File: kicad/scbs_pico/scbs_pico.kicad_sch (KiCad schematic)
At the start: 64 parts, among them J1 Conn_01x06_Male, J2 Conn_ARM_JTAG_SWD_10, Q1 2N2907, Q2 2N7002, Q3 MMBT3904, Q4 MMBT3904, U1 TLV9062xD, U2 PC817, U3 Pico

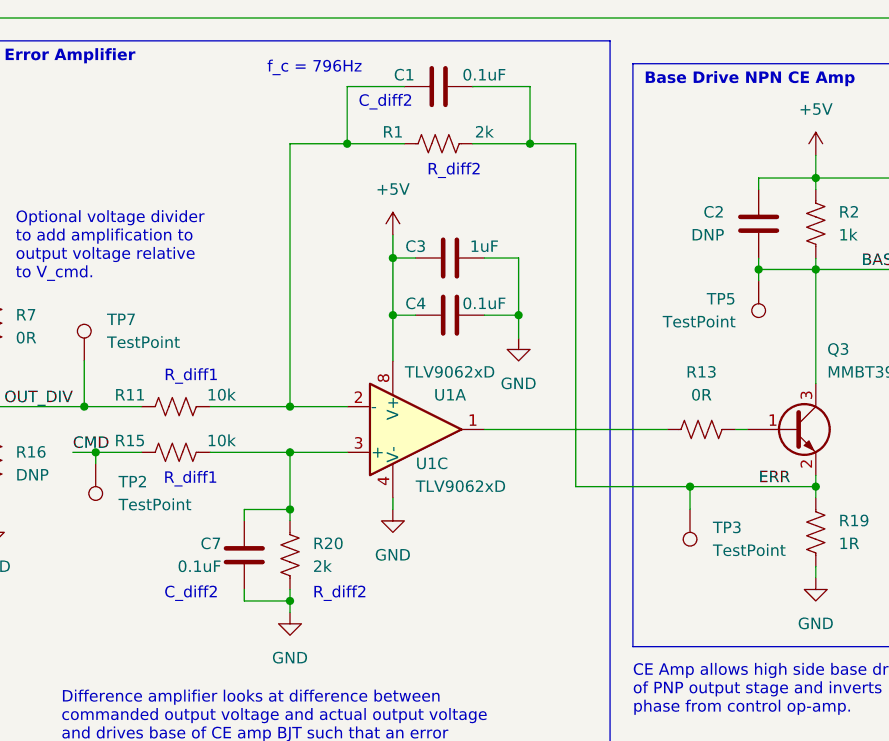
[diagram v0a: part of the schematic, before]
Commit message: Add calibrated output voltage setting
* Python script serial utility for sending DIS, MWR, MRD commands to
  device.
* Three-coefficient polynomial calibration implemented in firmware for
  closer matching of output voltage (looks pretty darn good)! Makes up
  for the crappiness / non-linearity of the PWM pseudo-DAC driving a
  load without a buffer.
* Connecting the plumbing for setting output voltage via serial in the
  SCBS firmware.
* Clean up some commented code garbage that was lying around.
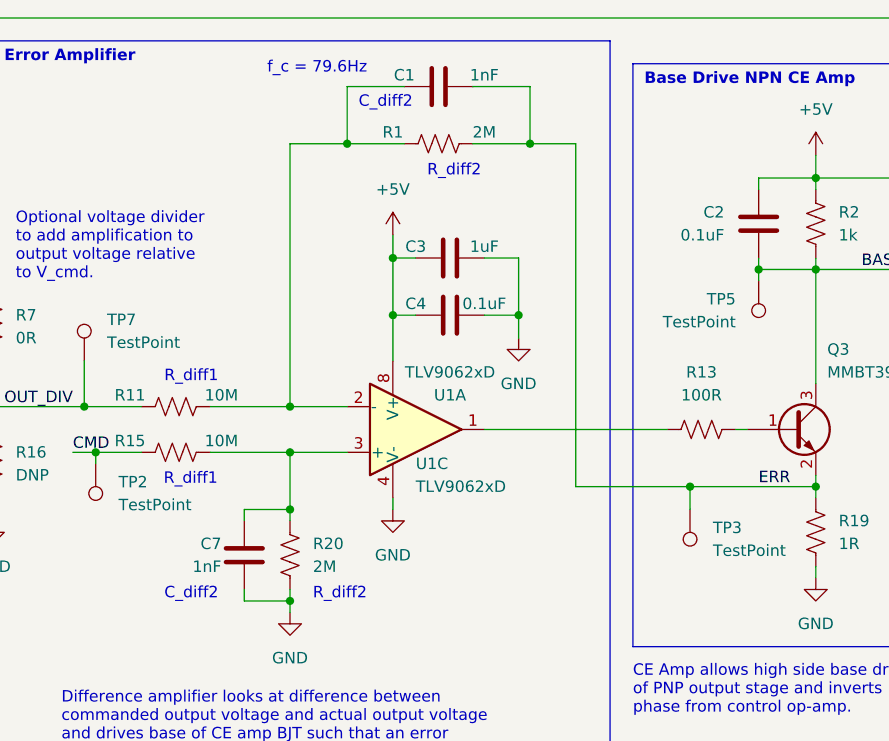
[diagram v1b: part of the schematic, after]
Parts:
- C1, C7: value 0.1uF -> 1nF
- C2: value DNP -> 0.1uF
- R1, R20: value 2k -> 2M
- R11, R15: value 10k -> 10M
- R13: value 0R -> 100R
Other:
- note added: "f_c = 79.6Hz"
- note removed: "f_c = 796Hz"
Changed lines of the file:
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@@
     (effects (font (size 1.27 1.27) bold) (justify left bottom))
   )
-  (text "f_c = 796Hz" (at 203.2 38.1 0)
+  (text "f_c = 79.6Hz" (at 203.2 38.1 0)
     (effects (font (size 1.27 1.27)) (justify left bottom))
   )
@@
     (in_bom yes) (on_board yes) (fields_autoplaced)
     (property "Reference" "R13" (id 0) (at 251.46 71.12 90))
-    (property "Value" "0R" (id 1) (at 251.46 73.66 90))
+    (property "Value" "100R" (id 1) (at 251.46 73.66 90))
     (property "Footprint" "Resistor_SMD:R_0805_2012Metric" (id 2) (at 251.714 76.454 90)
       (effects (font (size 1.27 1.27)) hide)
@@
     (in_bom yes) (on_board yes)
     (property "Reference" "C1" (id 0) (at 218.44 38.1 90))
-    (property "Value" "0.1uF" (id 1) (at 227.33 38.1 90))
+    (property "Value" "1nF" (id 1) (at 227.33 38.1 90))
     (property "Footprint" "Capacitor_SMD:C_0805_2012Metric" (id 2) (at 226.06 38.4048 0)
       (effects (font (size 1.27 1.27)) hide)
@@
     (in_bom yes) (on_board yes)
     (property "Reference" "R15" (id 0) (at 187.96 78.74 90))
-    (property "Value" "10k" (id 1) (at 198.12 78.74 90))
+    (property "Value" "10M" (id 1) (at 198.12 78.74 90))
     (property "Footprint" "Resistor_SMD:R_0805_2012Metric" (id 2) (at 193.294 78.994 90)
       (effects (font (size 1.27 1.27)) hide)
@@
     (in_bom yes) (on_board yes)
     (property "Reference" "R11" (id 0) (at 187.96 73.66 90))
-    (property "Value" "10k" (id 1) (at 198.12 73.66 90))
+    (property "Value" "10M" (id 1) (at 198.12 73.66 90))
     (property "Footprint" "Resistor_SMD:R_0805_2012Metric" (id 2) (at 193.294 73.914 90)
       (effects (font (size 1.27 1.27)) hide)
@@
       (effects (font (size 1.27 1.27)) (justify right))
     )
-    (property "Value" "0.1uF" (id 1) (at 198.12 92.71 0)
+    (property "Value" "1nF" (id 1) (at 198.12 92.71 0)
       (effects (font (size 1.27 1.27)) (justify right))
     )
@@
     (in_bom yes) (on_board yes)
     (property "Reference" "R1" (id 0) (at 217.17 44.45 90))
-    (property "Value" "2k" (id 1) (at 227.33 44.45 90))
+    (property "Value" "2M" (id 1) (at 227.33 44.45 90))
     (property "Footprint" "Resistor_SMD:R_0805_2012Metric" (id 2) (at 222.504 44.704 90)
       (effects (font (size 1.27 1.27)) hide)
@@
       (effects (font (size 1.27 1.27)) (justify left))
     )
-    (property "Value" "2k" (id 1) (at 208.28 92.7099 0)
+    (property "Value" "2M" (id 1) (at 208.28 92.7099 0)
       (effects (font (size 1.27 1.27)) (justify left))
     )
@@
       (effects (font (size 1.27 1.27)) (justify right))
     )
-    (property "Value" "DNP" (id 1) (at 254 55.88 0)
+    (property "Value" "0.1uF" (id 1) (at 254 55.88 0)
       (effects (font (size 1.27 1.27)) (justify right))
     )
@@
     )
     (path "/501c76a6-d2b9-4bd2-89b6-22fe1a20bdf8"
-      (reference "C1") (unit 1) (value "0.1uF") (footprint "Capacitor_SMD:C_0805_2012Metric")
+      (reference "C1") (unit 1) (value "1nF") (footprint "Capacitor_SMD:C_0805_2012Metric")
     )
     (path "/ea657372-77a3-4b71-8e5f-768a7eedd395"
-      (reference "C2") (unit 1) (value "DNP") (footprint "Capacitor_SMD:C_0805_2012Metric")
+      (reference "C2") (unit 1) (value "0.1uF") (footprint "Capacitor_SMD:C_0805_2012Metric")
     )
     (path "/81879832-ef3a-4d07-bc20-d7739a2f0b44"
@@
     )
     (path "/9977a2d0-eb1e-4053-9401-7449ac849cb7"
-      (reference "C7") (unit 1) (value "0.1uF") (footprint "Capacitor_SMD:C_0805_2012Metric")
+      (reference "C7") (unit 1) (value "1nF") (footprint "Capacitor_SMD:C_0805_2012Metric")
     )
     (path "/44978827-6e8d-4181-bf69-4f56262ac5b3"
@@
     )
     (path "/9df6450b-426e-44a8-8013-a148bb9d7476"
-      (reference "R1") (unit 1) (value "2k") (footprint "Resistor_SMD:R_0805_2012Metric")
+      (reference "R1") (unit 1) (value "2M") (footprint "Resistor_SMD:R_0805_2012Metric")
     )
     (path "/996fc4c6-670c-47e0-8fd9-40439fd4e145"
@@
     )
     (path "/89e2b305-09b7-42be-a849-0b21d2a4259b"
-      (reference "R11") (unit 1) (value "10k") (footprint "Resistor_SMD:R_0805_2012Metric")
+      (reference "R11") (unit 1) (value "10M") (footprint "Resistor_SMD:R_0805_2012Metric")
     )
     (path "/ff8d37cd-3da3-417c-a0fc-f4fdf44a9126"
@@
     )
     (path "/3da06448-3f74-4948-a6de-8e4ddcf3a451"
-      (reference "R13") (unit 1) (value "0R") (footprint "Resistor_SMD:R_0805_2012Metric")
+      (reference "R13") (unit 1) (value "100R") (footprint "Resistor_SMD:R_0805_2012Metric")
     )
     (path "/01aaca7e-4af3-469d-90de-3e450da96ed7"
@@
     )
     (path "/85853062-8be8-409c-8854-83e4a8ae9bfe"
-      (reference "R15") (unit 1) (value "10k") (footprint "Resistor_SMD:R_0805_2012Metric")
+      (reference "R15") (unit 1) (value "10M") (footprint "Resistor_SMD:R_0805_2012Metric")
     )
     (path "/59a896a2-1a0f-4726-81bd-86b5c1073d52"
@@
     )
     (path "/9f1e2e01-723a-446f-8f13-e29292866f46"
-      (reference "R20") (unit 1) (value "2k") (footprint "Resistor_SMD:R_0805_2012Metric")
+      (reference "R20") (unit 1) (value "2M") (footprint "Resistor_SMD:R_0805_2012Metric")
     )
     (path "/fc0f4a6b-8c97-40be-a956-b8dcc5258115"

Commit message: Add SCBS array PCBA Rev A
* Update design notebook.
* Export some stuff for SCBS Pico.
* Create SCBS Array motherboard.
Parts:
- added C?: 10uF 16V, symbol Device:C_Polarized_US
- C2: value 0.1uF -> DNP
- R5: value 100R -> 750R
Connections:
- net GND: now also C?.2
- net OUT: now also C?.1
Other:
- note added: "Output Cap (Electrolytic)"
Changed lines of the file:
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@@
   (junction (at 295.91 83.82) (diameter 0) (color 0 0 0 0)
   )
+  (junction (at 379.73 69.85) (diameter 0) (color 0 0 0 0)
+  )
   (junction (at 341.63 116.84) (diameter 0) (color 0 0 0 0)
   )
@@
     (stroke (width 0) (type default) (color 0 0 0 0))
   )
+  (wire (pts (xy 379.73 80.01) (xy 379.73 82.55))
+    (stroke (width 0) (type default) (color 0 0 0 0))
+  )
   (wire (pts (xy 168.91 171.45) (xy 168.91 170.18))
     (stroke (width 0) (type default) (color 0 0 0 0))
@@
     (stroke (width 0) (type default) (color 0 0 0 0))
   )
-  (wire (pts (xy 374.65 69.85) (xy 388.62 69.85))
+  (wire (pts (xy 374.65 69.85) (xy 379.73 69.85))
     (stroke (width 0) (type default) (color 0 0 0 0))
   )
@@
     (stroke (width 0) (type default) (color 0 0 0 0))
   )
+  (wire (pts (xy 379.73 69.85) (xy 388.62 69.85))
+    (stroke (width 0) (type default) (color 0 0 0 0))
+  )
   (wire (pts (xy 217.17 55.88) (xy 217.17 58.42))
     (stroke (width 0) (type default) (color 0 0 0 0))
@@
     (stroke (width 0) (type default) (color 0 0 0 0))
   )
+  (wire (pts (xy 379.73 69.85) (xy 379.73 72.39))
+    (stroke (width 0) (type default) (color 0 0 0 0))
+  )
   (wire (pts (xy 111.76 104.14) (xy 114.3 104.14))
     (stroke (width 0) (type default) (color 0 0 0 0))
@@
     (effects (font (size 1.27 1.27)) (justify left bottom))
   )
+  (text "Output Cap\n(Electrolytic)" (at 383.54 82.55 0)
+    (effects (font (size 1.27 1.27)) (justify left bottom))
+  )
   (text "I_f = 10mA for >100% CTR\nV_f = 1.2V" (at 104.14 95.25 0)
     (effects (font (size 1.27 1.27)) (justify left bottom))
@@
     (in_bom yes) (on_board yes) (fields_autoplaced)
     (property "Reference" "R5" (id 0) (at 283.21 53.34 90))
-    (property "Value" "100R" (id 1) (at 283.21 55.88 90))
+    (property "Value" "750R" (id 1) (at 283.21 55.88 90))
     (property "Footprint" "Resistor_SMD:R_0805_2012Metric" (id 2) (at 283.464 58.674 90)
       (effects (font (size 1.27 1.27)) hide)
@@
     (pin "1")
   )
+  (symbol (lib_id "Device:C_Polarized_US") (at 379.73 76.2 0) (unit 1)
+    (in_bom yes) (on_board yes) (fields_autoplaced)
+    (property "Reference" "C?" (id 0) (at 383.54 74.2949 0)
+      (effects (font (size 1.27 1.27)) (justify left))
+    )
+    (property "Value" "10uF 16V" (id 1) (at 383.54 76.8349 0)
+      (effects (font (size 1.27 1.27)) (justify left))
+    )
+    (property "Footprint" "" (id 2) (at 379.73 76.2 0)
+      (effects (font (size 1.27 1.27)) hide)
+    )
+    (property "Datasheet" "~" (id 3) (at 379.73 76.2 0)
+      (effects (font (size 1.27 1.27)) hide)
+    )
+    (pin "1")
+    (pin "2")
+  )
   (symbol (lib_id "Device:C") (at 247.65 212.09 0) (unit 1)
     (in_bom yes) (on_board yes) (fields_autoplaced)
@@
     (pin "3")
   )
+  (symbol (lib_id "power:GND") (at 379.73 82.55 0) (unit 1)
+    (in_bom yes) (on_board yes) (fields_autoplaced)
+    (property "Reference" "#PWR?" (id 0) (at 379.73 88.9 0)
+      (effects (font (size 1.27 1.27)) hide)
+    )
+    (property "Value" "GND" (id 1) (at 379.73 87.63 0))
+    (property "Footprint" "" (id 2) (at 379.73 82.55 0)
+      (effects (font (size 1.27 1.27)) hide)
+    )
+    (property "Datasheet" "" (id 3) (at 379.73 82.55 0)
+      (effects (font (size 1.27 1.27)) hide)
+    )
+    (pin "1")
+  )
   (symbol (lib_id "Device:R_US") (at 355.6 99.06 0) (unit 1)
     (in_bom yes) (on_board yes) (fields_autoplaced)
@@
       (effects (font (size 1.27 1.27)) (justify right))
     )
-    (property "Value" "0.1uF" (id 1) (at 254 55.88 0)
+    (property "Value" "DNP" (id 1) (at 254 55.88 0)
       (effects (font (size 1.27 1.27)) (justify right))
     )
@@
       (reference "#PWR0130") (unit 1) (value "GND") (footprint "")
     )
+    (path "/35b9a854-62cb-49e7-9c9d-3e326983e03c"
+      (reference "#PWR?") (unit 1) (value "GND") (footprint "")
+    )
     (path "/501c76a6-d2b9-4bd2-89b6-22fe1a20bdf8"
       (reference "C1") (unit 1) (value "1nF") (footprint "Capacitor_SMD:C_0805_2012Metric")
     )
     (path "/ea657372-77a3-4b71-8e5f-768a7eedd395"
-      (reference "C2") (unit 1) (value "0.1uF") (footprint "Capacitor_SMD:C_0805_2012Metric")
+      (reference "C2") (unit 1) (value "DNP") (footprint "Capacitor_SMD:C_0805_2012Metric")
     )
     (path "/81879832-ef3a-4d07-bc20-d7739a2f0b44"
@@
       (reference "C9") (unit 1) (value "0.1uF") (footprint "Capacitor_SMD:C_0805_2012Metric")
     )
+    (path "/310f666a-ea20-449f-a9c3-eff3281f36ff"
+      (reference "C?") (unit 1) (value "10uF 16V") (footprint "")
+    )
     (path "/5183dd08-31e0-4338-a196-36de3f7fb976"
       (reference "D1") (unit 1) (value "1N4148") (footprint "Diode_SMD:D_SOD-123")
@@
     )
     (path "/01c7dbf1-4f72-4a80-838a-95b588865507"
-      (reference "R5") (unit 1) (value "100R") (footprint "Resistor_SMD:R_0805_2012Metric")
+      (reference "R5") (unit 1) (value "750R") (footprint "Resistor_SMD:R_0805_2012Metric")
     )
     (path "/52915bd2-415a-4400-b972-3830f62c9437"

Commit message: SCBS Array design, add single cell packets
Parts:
- R10, R8, R9: value 4R 1% 0805 -> 3.9R 1% 0805
- R12: value 4R 1% 0805 -> 4.3R 1% 0805
- R17, R18: value 500k 0.1% -> 510k 1%
- R21, R22: value 8.25M 0.1% -> 8.2M 1%
- R5: value 750R -> 510R
- gave numbers to parts that had none: 1
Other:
- moved on the sheet: R10, R12, R8, R9
